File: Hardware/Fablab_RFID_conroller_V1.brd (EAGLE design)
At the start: 97 x 64 mm, 47 parts, among them IC1 V_REG_LDOSMD, J1 JACK-DC-3P-3410020P1

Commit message: Address erratum: Fix +5V connection of relay coil.
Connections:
- removed net N$10: D1.C, REL1.COIL1
- net +5V: now also D1.C, REL1.COIL1
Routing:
- net +5V: track 102.4 -> 201.3 mm
- net N$10: track 6.45 -> 0.00 mm
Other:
- board text added: "VERSION 1.1"
- board text removed: "VERSION 1"
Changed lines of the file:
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@@
 FABLAB WINTERTHUR
 20. MAY 2017</text>
-<text x="74.2" y="1.6" size="1.4224" layer="25" font="vector" ratio="22">VERSION 1</text>
+<text x="74.2" y="1.6" size="1.4224" layer="25" font="vector" ratio="22">VERSION 1.1</text>
 <rectangle x1="34.6356" y1="23.34" x2="35.042" y2="23.4416" layer="26" rot="R90"/>
 <rectangle x1="34.6864" y1="24.2036" x2="34.9912" y2="24.3052" layer="26" rot="R90"/>
@@
 <polygon width="0.254" layer="1" isolate="0.3" orphans="yes">
 <vertex x="66" y="43.5"/>
-<vertex x="58" y="43.5"/>
-<vertex x="56" y="41.5"/>
+<vertex x="56" y="43.5"/>
 <vertex x="56" y="8"/>
 <vertex x="52" y="4"/>
@@
 <wire x1="14.088" y1="13.284" x2="18.088" y2="10.088" width="0.2032" layer="1"/>
 <wire x1="18.088" y1="10.088" x2="18.5" y2="10.5" width="0.2032" layer="1"/>
-<wire x1="46.19" y1="9.22" x2="65.9" y2="43" width="0" layer="19" extent="1-1"/>
-<wire x1="28.19" y1="5" x2="46" y2="5" width="0" layer="19" extent="16-16"/>
+<contactref element="D1" pad="C"/>
+<contactref element="REL1" pad="COIL1"/>
+<wire x1="53.39" y1="49.12" x2="56.4" y2="49.12" width="0.8128" layer="1"/>
+<wire x1="56.4" y1="49.12" x2="56.74" y2="49.12" width="0.8128" layer="1"/>
+<wire x1="56.74" y1="49.12" x2="57.404" y2="49.784" width="0.8128" layer="1"/>
+<wire x1="57.404" y1="49.784" x2="59.516" y2="49.784" width="0.8128" layer="1"/>
+<wire x1="59.516" y1="49.784" x2="59.55" y2="49.75" width="0.8128" layer="1"/>
+<wire x1="56.4" y1="49.12" x2="56.4" y2="43.2" width="0.8128" layer="1"/>
+<wire x1="56.4" y1="43.2" x2="56.4" y2="12" width="0.8128" layer="1"/>
+<wire x1="56.4" y1="12" x2="60.4" y2="8" width="0.8128" layer="1"/>
+<wire x1="60.4" y1="8" x2="60.4" y2="4" width="0.8128" layer="1"/>
+<wire x1="60.4" y1="4" x2="58" y2="1.6" width="0.8128" layer="1"/>
+<wire x1="58" y1="1.6" x2="29.2" y2="1.6" width="0.8128" layer="1"/>
+<wire x1="29.2" y1="1.6" x2="28.19" y2="2.61" width="0.8128" layer="1"/>
+<wire x1="28.19" y1="2.61" x2="28.19" y2="5" width="0.8128" layer="1"/>
+<wire x1="56.4" y1="43.2" x2="66.1" y2="43.2" width="0.8128" layer="1"/>
 </signal>
 <signal name="+3V3">
@@
 <wire x1="62.992" y1="49.792" x2="62.95" y2="49.75" width="0.8128" layer="1"/>
 </signal>
-<signal name="N$10">
-<contactref element="D1" pad="C"/>
-<contactref element="REL1" pad="COIL1"/>
-<wire x1="53.39" y1="49.12" x2="56.74" y2="49.12" width="0.8128" layer="1"/>
-<wire x1="56.74" y1="49.12" x2="57.404" y2="49.784" width="0.8128" layer="1"/>
-<wire x1="57.404" y1="49.784" x2="59.516" y2="49.784" width="0.8128" layer="1"/>
-<wire x1="59.516" y1="49.784" x2="59.55" y2="49.75" width="0.8128" layer="1"/>
-</signal>
 <signal name="N$13">

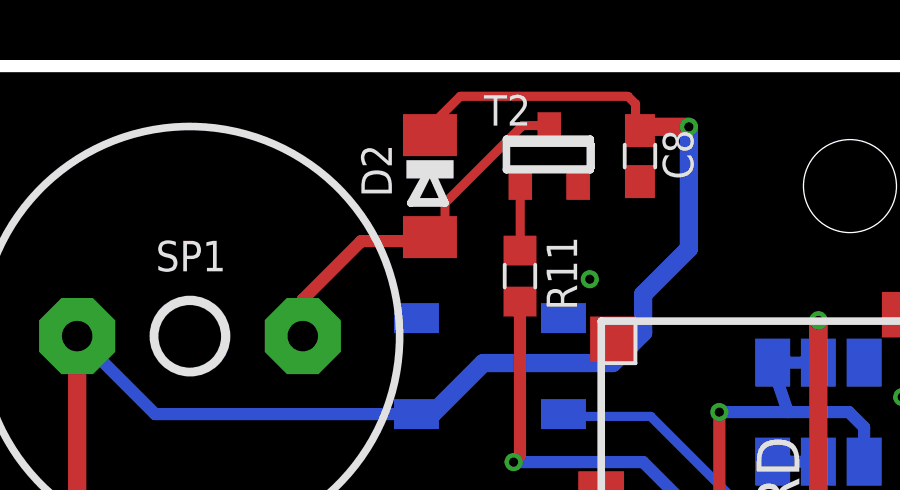
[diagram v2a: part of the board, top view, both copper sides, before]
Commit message: Address erratum: Replace diode D2 by 10k resistor R13.
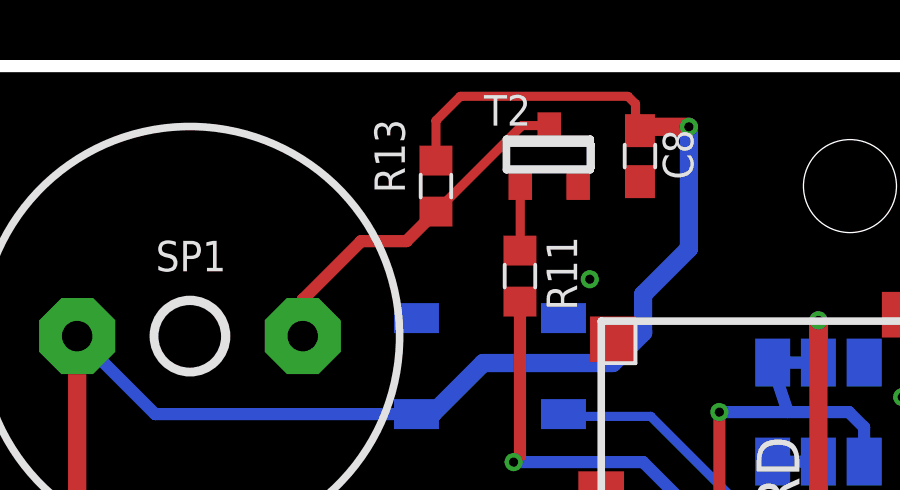
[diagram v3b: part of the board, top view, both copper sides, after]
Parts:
- removed D2: (no value), diode:MINIMELF
- added R13: 10k, resistor:R0603
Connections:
- net +5V: now also R13.2; no longer D2.C
- net N$8: now also R13.1; no longer D2.A
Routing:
- net +5V: track 201.3 -> 202.1 mm
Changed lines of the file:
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@@
 <wire x1="61.722" y1="50.292" x2="61.722" y2="49.149" width="0.254" layer="25"/>
 <wire x1="61.722" y1="49.149" x2="60.579" y2="49.784" width="0.254" layer="25"/>
-<wire x1="79.629" y1="60.579" x2="78.994" y2="60.579" width="0.254" layer="25"/>
-<wire x1="78.994" y1="60.579" x2="78.359" y2="60.579" width="0.254" layer="25"/>
-<wire x1="78.994" y1="60.579" x2="79.502" y2="59.436" width="0.254" layer="25"/>
-<wire x1="79.502" y1="59.436" x2="78.359" y2="59.436" width="0.254" layer="25"/>
-<wire x1="78.359" y1="59.436" x2="78.994" y2="60.579" width="0.254" layer="25"/>
 <wire x1="59.563" y1="61.468" x2="62.357" y2="61.468" width="0.254" layer="25"/>
 <wire x1="62.357" y1="61.468" x2="62.357" y2="60.452" width="0.254" layer="25"/>
@@
 <attribute name="VALUE" x="83.905" y="56.365" size="1.27" layer="27" rot="R90"/>
 </element>
-<element name="D2" library="diode" package="MINIMELF" value="" x="79" y="60" smashed="yes" rot="R270">
-<attribute name="NAME" x="76.714" y="61.397" size="1.016" layer="25" font="vector" ratio="22" rot="R270"/>
-<attribute name="VALUE" x="76.587" y="61.651" size="1.27" layer="27" rot="R270"/>
-</element>
 <element name="C8" library="resistor" package="C0603" value="100nF" x="86" y="61" smashed="yes" rot="R270">
 <attribute name="NAME" x="86.762" y="61.889" size="1.016" layer="25" font="vector" ratio="22" rot="R270"/>
@@
 </element>
 <element name="U$6" library="logos" package="OSHW-LOGO-L" value="" x="61.95" y="3.45"/>
+<element name="R13" library="resistor" package="R0603" value="10k" x="79.2" y="60" smashed="yes" rot="R90">
+<attribute name="NAME" x="78.165" y="59.765" size="1.016" layer="25" font="vector" ratio="22" rot="R90"/>
+<attribute name="VALUE" x="81.105" y="59.365" size="1.27" layer="27" rot="R90"/>
+</element>
 </elements>
 <signals>
@@
 <contactref element="JP2" pad="1"/>
 <contactref element="U$2" pad="J1.5"/>
-<contactref element="D2" pad="C"/>
 <contactref element="SP1" pad="1"/>
 <contactref element="C8" pad="1"/>
@@
 <wire x1="87.63" y1="61.976" x2="86.126" y2="61.976" width="0.6096" layer="1"/>
 <wire x1="86.126" y1="61.976" x2="86" y2="61.85" width="0.6096" layer="1"/>
-<wire x1="79" y1="61.7" x2="79" y2="61.982" width="0.3048" layer="1"/>
-<wire x1="79" y1="61.982" x2="80.01" y2="62.992" width="0.3048" layer="1"/>
 <wire x1="80.01" y1="62.992" x2="85.598" y2="62.992" width="0.3048" layer="1"/>
 <wire x1="85.598" y1="62.992" x2="85.852" y2="62.738" width="0.3048" layer="1"/>
@@
 <wire x1="28.19" y1="2.61" x2="28.19" y2="5" width="0.8128" layer="1"/>
 <wire x1="56.4" y1="43.2" x2="66.1" y2="43.2" width="0.8128" layer="1"/>
+<contactref element="R13" pad="2"/>
+<wire x1="80.01" y1="62.992" x2="79.2" y2="62.182" width="0.3048" layer="1"/>
+<wire x1="79.2" y1="62.182" x2="79.2" y2="60.85" width="0.3048" layer="1"/>
 </signal>
 <signal name="+3V3">
@@
 <contactref element="T2" pad="1"/>
 <contactref element="SP1" pad="2"/>
-<contactref element="D2" pad="A"/>
-<wire x1="82.9746" y1="62.016" x2="82.082" y2="62.016" width="0.3048" layer="1"/>
-<wire x1="82.082" y1="62.016" x2="79.502" y2="59.436" width="0.3048" layer="1"/>
-<wire x1="79.502" y1="59.436" x2="79.502" y2="58.802" width="0.3048" layer="1"/>
-<wire x1="79.502" y1="58.802" x2="79" y2="58.3" width="0.3048" layer="1"/>
+<wire x1="82.9746" y1="62.016" x2="82.066" y2="62.016" width="0.3048" layer="1"/>
 <wire x1="74.7592" y1="55" x2="74.7592" y2="56.2172" width="0.4064" layer="1"/>
 <wire x1="74.7592" y1="56.2172" x2="76.708" y2="58.166" width="0.4064" layer="1"/>
-<wire x1="76.708" y1="58.166" x2="78.866" y2="58.166" width="0.4064" layer="1"/>
-<wire x1="78.866" y1="58.166" x2="79" y2="58.3" width="0.4064" layer="1"/>
+<contactref element="R13" pad="1"/>
+<wire x1="76.708" y1="58.166" x2="78.216" y2="58.166" width="0.4064" layer="1"/>
+<wire x1="78.216" y1="58.166" x2="79.2" y2="59.15" width="0.4064" layer="1"/>
+<wire x1="79.2" y1="59.15" x2="79.216" y2="59.15" width="0.4064" layer="1"/>
+<wire x1="82.066" y1="62.016" x2="79.2" y2="59.15" width="0.3048" layer="1"/>
 </signal>
 <signal name="N$11">
